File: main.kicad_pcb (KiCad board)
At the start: 2 copper layers, 29.2 x 32.5 mm, 2 parts, among them P1 CONN_02X10, P2 CONN_02X10

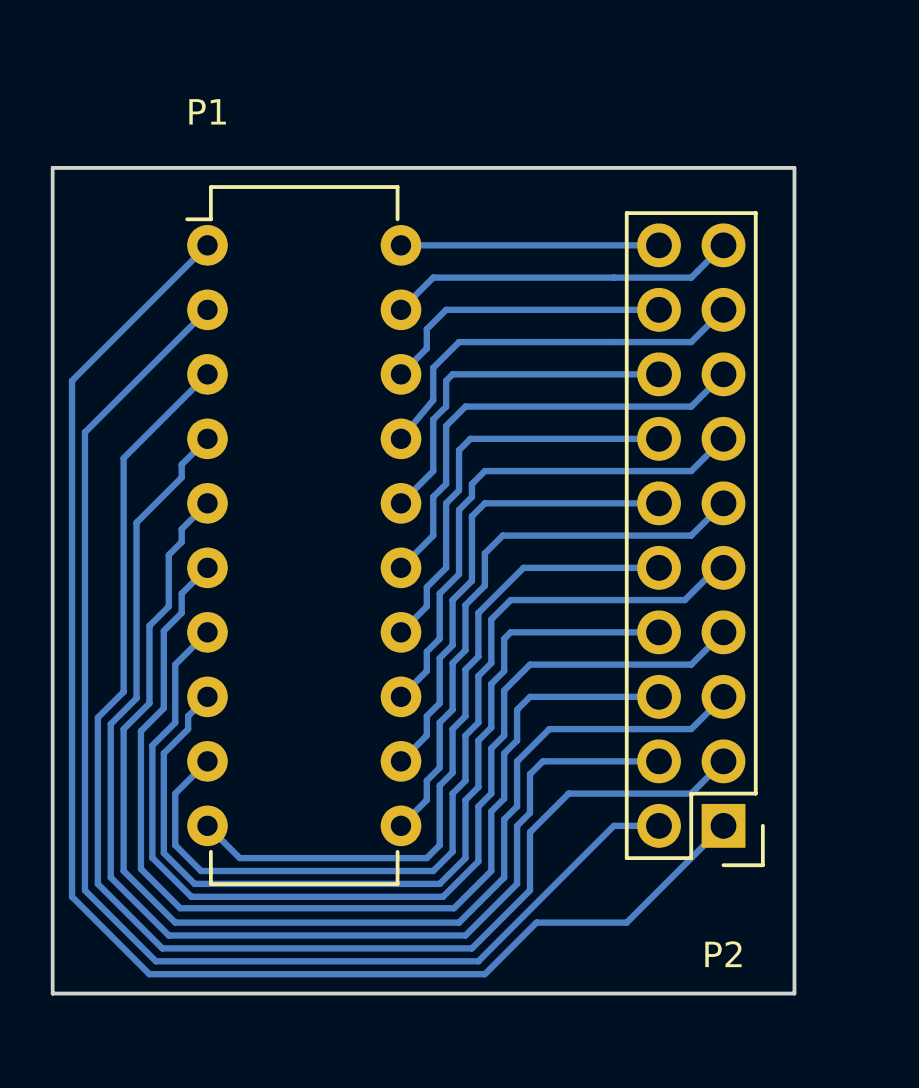
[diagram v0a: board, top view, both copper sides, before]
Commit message: change pcb layout
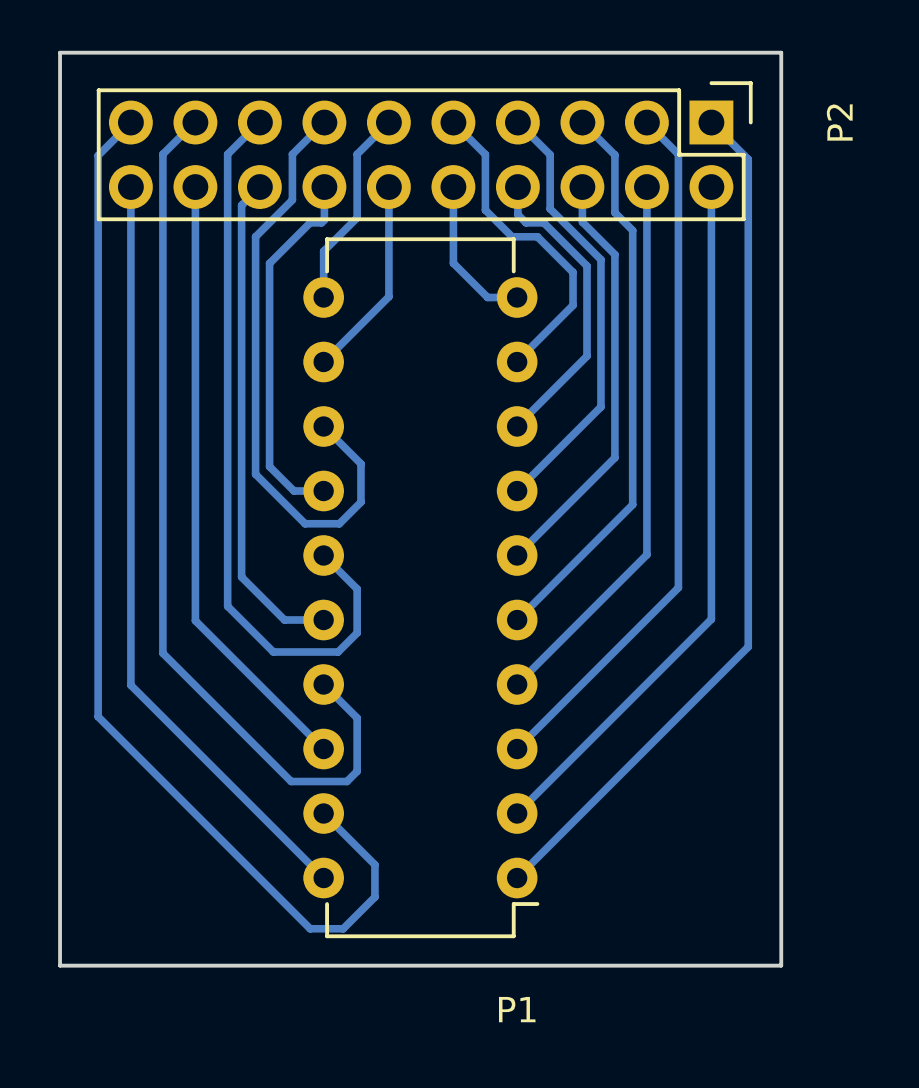
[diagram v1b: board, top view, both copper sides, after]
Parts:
- moved P1 27.7 mm to (174.5, 128.8), turned to 180 degrees
- moved P2 27.7 mm to (182.2, 99.0), turned to 270 degrees
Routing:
- net Net-(P1-Pad19): track 13.8 -> 42.9 mm
- net Net-(P1-Pad4): track 46.5 -> 21.7 mm
- net Net-(P1-Pad3): track 51.9 -> 27.8 mm
- net Net-(P1-Pad5): track 46.4 -> 22.3 mm
- net Net-(P1-Pad6): track 40.6 -> 16.6 mm
- net Net-(P1-Pad7): track 40.6 -> 17.2 mm
- net Net-(P1-Pad1): track 57.2 -> 34.1 mm
- net Net-(P1-Pad8): track 35.1 -> 12.1 mm
- net Net-(P1-Pad2): track 50.8 -> 27.8 mm
- net Net-(P1-Pad9): track 35.2 -> 12.9 mm
- net Net-(P1-Pad10): track 27.5 -> 6.07 mm
- net Net-(P1-Pad20): track 10.2 -> 30.4 mm
- net Net-(P1-Pad17): track 15.6 -> 35.7 mm
- net Net-(P1-Pad11): track 22.3 -> 7.95 mm
- net Net-(P1-Pad18): track 11.7 -> 24.2 mm
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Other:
- board size 29.2 x 32.5 mm -> 28.4 x 36 mm
- net class Default: trace_width 0.25 -> 0.3
